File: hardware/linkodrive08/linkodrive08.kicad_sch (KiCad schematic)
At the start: 146 parts, among them J1 USB_C_Receptacle_USB2.0_16P, J10 WCH_GPIO, J11 ENC, J12 LKS_SPI, J13 LKS_I2C, J14 WCH_UART_ALT, J15 LKS_SIF, J16 LKS_IO, J2 HALL, J3 WCH_SWD, J4 LKS_SWD, J5 MOT_POWER, J6 GATE_DRIVE, J7 LOGIC_POWER, J8 MOT, J9 CAN, Q1 HSU6066, Q2 HSU6066, Q3 HSU6066, Q4 HSU6066, Q5 HSU6066, Q6 HSU6066, U1 LKS32MC086NxQx, U2 CH32V203G6U6, U3 XL1509-ADJ, U4 SN65HVD230, U5 LGS5145, Y1 Crystal_GND24_Small

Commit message: Work on pcb and some parts changes
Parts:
- C33, C34, C35: footprint MISSING -> Capacitor_SMD:C_Elec_10x10.2
- D1, D10, D4, D7: value SS34 -> C28646289; footprint Diode_SMD:D_SMA -> Diode_SMD:D_SOD-123F; LCSC C8678 -> C28646289
- D2, D3, D5, D6, D8, D9: value ES2DB -> ES2JW; footprint Diode_SMD:D_SMB -> Diode_SMD:D_SOD-123F; LCSC C162764 -> C353499
- Q1, Q2, Q3, Q4, Q5, Q6: footprint Package_TO_SOT_SMD:TO-252-2 -> Package_SO:ONSemi_SO-8FL_488AA
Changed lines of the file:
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@@
 			)
 		)
-		(property "Footprint" "Package_TO_SOT_SMD:TO-252-2"
+		(property "Footprint" "Package_SO:ONSemi_SO-8FL_488AA"
 			(at 327.66 198.12 0)
 			(effects
@@
 			)
 		)
-		(property "Footprint" "MISSING"
+		(property "Footprint" "Capacitor_SMD:C_Elec_10x10.2"
 			(at 251.46 167.64 0)
 			(effects
@@
 			)
 		)
-		(property "Value" "SS34"
+		(property "Value" "C28646289"
 			(at 285.75 181.61 0)
 			(effects
@@
 			)
 		)
-		(property "Footprint" "Diode_SMD:D_SMA"
+		(property "Footprint" "Diode_SMD:D_SOD-123F"
 			(at 280.67 184.15 90)
 			(effects
@@
 			)
 		)
-		(property "LCSC" "C8678"
+		(property "LCSC" "C28646289"
 			(at 280.67 184.15 90)
 			(effects
@@
 			)
 		)
-		(property "Value" "ES2DB"
+		(property "Value" "ES2JW"
 			(at 294.132 211.074 0)
 			(effects
@@
 			)
 		)
-		(property "Footprint" "Diode_SMD:D_SMB"
+		(property "Footprint" "Diode_SMD:D_SOD-123F"
 			(at 297.18 213.36 90)
 			(effects
@@
 			)
 		)
-		(property "LCSC" "C162764"
+		(property "LCSC" "C353499"
 			(at 297.18 213.36 0)
 			(effects
@@
 			)
 		)
-		(property "Value" "ES2DB"
+		(property "Value" "ES2JW"
 			(at 167.132 264.414 0)
 			(effects
@@
 			)
 		)
-		(property "Footprint" "Diode_SMD:D_SMB"
+		(property "Footprint" "Diode_SMD:D_SOD-123F"
 			(at 170.18 266.7 90)
 			(effects
@@
 			)
 		)
-		(property "LCSC" "C162764"
+		(property "LCSC" "C353499"
 			(at 170.18 266.7 0)
 			(effects
@@
 			)
 		)
-		(property "Footprint" "Package_TO_SOT_SMD:TO-252-2"
+		(property "Footprint" "Package_SO:ONSemi_SO-8FL_488AA"
 			(at 200.66 264.16 0)
 			(effects
@@
 			)
 		)
-		(property "Value" "ES2DB"
+		(property "Value" "ES2JW"
 			(at 165.862 211.074 0)
 			(effects
@@
 			)
 		)
-		(property "Footprint" "Diode_SMD:D_SMB"
+		(property "Footprint" "Diode_SMD:D_SOD-123F"
 			(at 168.91 213.36 90)
 			(effects
@@
 			)
 		)
-		(property "LCSC" "C162764"
+		(property "LCSC" "C353499"
 			(at 168.91 213.36 0)
 			(effects
@@
 			)
 		)
-		(property "Footprint" "Package_TO_SOT_SMD:TO-252-2"
+		(property "Footprint" "Package_SO:ONSemi_SO-8FL_488AA"
 			(at 327.66 210.82 0)
 			(effects
@@
 			)
 		)
-		(property "Value" "SS34"
+		(property "Value" "C28646289"
 			(at 358.902 49.784 90)
 			(effects
@@
 			)
 		)
-		(property "Footprint" "Diode_SMD:D_SMA"
+		(property "Footprint" "Diode_SMD:D_SOD-123F"
 			(at 355.6 48.26 90)
 			(effects
@@
 			)
 		)
-		(property "LCSC" "C8678"
+		(property "LCSC" "C28646289"
 			(at 355.6 48.26 90)
 			(effects
@@
 			)
 		)
-		(property "Footprint" "MISSING"
+		(property "Footprint" "Capacitor_SMD:C_Elec_10x10.2"
 			(at 227.33 167.64 0)
 			(effects
@@
 			)
 		)
-		(property "Value" "ES2DB"
+		(property "Value" "ES2JW"
 			(at 295.402 198.374 0)
 			(effects
@@
 			)
 		)
-		(property "Footprint" "Diode_SMD:D_SMB"
+		(property "Footprint" "Diode_SMD:D_SOD-123F"
 			(at 297.18 200.66 90)
 			(effects
@@
 			)
 		)
-		(property "LCSC" "C162764"
+		(property "LCSC" "C353499"
 			(at 297.18 200.66 0)
 			(effects
@@
 			)
 		)
-		(property "Footprint" "Package_TO_SOT_SMD:TO-252-2"
+		(property "Footprint" "Package_SO:ONSemi_SO-8FL_488AA"
 			(at 199.39 198.12 0)
 			(effects
@@
 			)
 		)
-		(property "Footprint" "MISSING"
+		(property "Footprint" "Capacitor_SMD:C_Elec_10x10.2"
 			(at 240.03 167.64 0)
 			(effects
@@
 			)
 		)
-		(property "Value" "SS34"
+		(property "Value" "C28646289"
 			(at 158.75 234.95 0)
 			(effects
@@
 			)
 		)
-		(property "Footprint" "Diode_SMD:D_SMA"
+		(property "Footprint" "Diode_SMD:D_SOD-123F"
 			(at 153.67 237.49 90)
 			(effects
@@
 			)
 		)
-		(property "LCSC" "C8678"
+		(property "LCSC" "C28646289"
 			(at 153.67 237.49 90)
 			(effects
@@
 			)
 		)
-		(property "Footprint" "Package_TO_SOT_SMD:TO-252-2"
+		(property "Footprint" "Package_SO:ONSemi_SO-8FL_488AA"
 			(at 200.66 251.46 0)
 			(effects
@@
 			)
 		)
-		(property "Value" "SS34"
+		(property "Value" "C28646289"
 			(at 157.48 181.61 0)
 			(effects
@@
 			)
 		)
-		(property "Footprint" "Diode_SMD:D_SMA"
+		(property "Footprint" "Diode_SMD:D_SOD-123F"
 			(at 152.4 184.15 90)
 			(effects
@@
 			)
 		)
-		(property "LCSC" "C8678"
+		(property "LCSC" "C28646289"
 			(at 152.4 184.15 90)
 			(effects
@@
 			)
 		)
-		(property "Value" "ES2DB"
+		(property "Value" "ES2JW"
 			(at 167.132 198.374 0)
 			(effects
@@
 			)
 		)
-		(property "Footprint" "Diode_SMD:D_SMB"
+		(property "Footprint" "Diode_SMD:D_SOD-123F"
 			(at 168.91 200.66 90)
 			(effects
@@
 			)
 		)
-		(property "LCSC" "C162764"
+		(property "LCSC" "C353499"
 			(at 168.91 200.66 0)
 			(effects
@@
 			)
 		)
-		(property "Footprint" "Package_TO_SOT_SMD:TO-252-2"
+		(property "Footprint" "Package_SO:ONSemi_SO-8FL_488AA"
 			(at 199.39 210.82 0)
 			(effects
@@
 			)
 		)
-		(property "Value" "ES2DB"
+		(property "Value" "ES2JW"
 			(at 168.402 251.714 0)
 			(effects
@@
 			)
 		)
-		(property "Footprint" "Diode_SMD:D_SMB"
+		(property "Footprint" "Diode_SMD:D_SOD-123F"
 			(at 170.18 254 90)
 			(effects
@@
 			)
 		)
-		(property "LCSC" "C162764"
+		(property "LCSC" "C353499"
 			(at 170.18 254 0)
 			(effects

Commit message: more work on PCB
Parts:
- added Q7: DMN3008SFG, Package_SON:Diodes_PowerDI3333-8, symbol Transistor_FET:DMN3008SFG
- D1, D10, D4, D7: value C28646289 -> DSK310
- U2: footprint Package_DFN_QFN:QFN-28-1EP_4x4mm_P0.4mm_EP2.6x2.6mm -> Package_DFN_QFN:QFN-28-1EP_4x4mm_P0.4mm_EP2.6x2.6mm_ThermalVias
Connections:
- new net: Q7.1 (S), Q7.2 (S), Q7.3 (S)
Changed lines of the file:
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@@
 			)
 		)
-		(property "Value" "C28646289"
+		(property "Value" "DSK310"
 			(at 285.75 181.61 0)
 			(effects
@@
 		)
 		(instances
-			(project ""
+			(project "linkodrive08"
 				(path "/1d70325a-38b2-49fb-b3a9-bb06bd833a17"
 					(reference "R44")
@@
 	)
 	(symbol
+		(lib_id "Transistor_FET:DMN3008SFG")
+		(at 330.2 184.15 0)
+		(unit 1)
+		(exclude_from_sim no)
+		(in_bom yes)
+		(on_board yes)
+		(dnp no)
+		(fields_autoplaced yes)
+		(property "Reference" "Q7"
+			(at 336.55 182.8799 0)
+			(effects
+				(font
+					(size 1.27 1.27)
+				)
+				(justify left)
+			)
+		)
+		(property "Value" "DMN3008SFG"
+			(at 336.55 185.4199 0)
+			(effects
+				(font
+					(size 1.27 1.27)
+				)
+				(justify left)
+			)
+		)
+		(property "Footprint" "Package_SON:Diodes_PowerDI3333-8"
+			(at 335.28 186.055 0)
+			(effects
+				(font
+					(size 1.27 1.27)
+					(italic yes)
+				)
+				(justify left)
+				(hide yes)
+			)
+		)
+		(property "Datasheet" "https://www.diodes.com/assets/Datasheets/DMN3008SFG.pdf"
+			(at 335.28 187.96 0)
+			(effects
+				(font
+					(size 1.27 1.27)
+				)
+				(justify left)
+				(hide yes)
+			)
+		)
+		(property "Description" "17.6A Id, 30V Vds, N-Channel Power MOSFET, 4.4mOhm Ron, 86nC Qg (typ), PowerDI3333-8"
+			(at 330.2 184.15 0)
+			(effects
+				(font
+					(size 1.27 1.27)
+				)
+				(hide yes)
+			)
+		)
+		(pin "3"
+		)
+		(pin "4"
+		)
+		(pin "2"
+		)
+		(pin "1"
+		)
+		(pin "5"
+		)
+		(instances
+			(project "linkodrive08"
+				(path "/1d70325a-38b2-49fb-b3a9-bb06bd833a17"
+					(reference "Q7")
+					(unit 1)
+				)
+			)
+		)
+	)
+	(symbol
 		(lib_id "Device:R_Small")
 		(at 346.71 224.79 270)
@@
 			)
 		)
-		(property "Value" "C28646289"
+		(property "Value" "DSK310"
 			(at 358.902 49.784 90)
 			(effects
@@
 			)
 		)
-		(property "Footprint" "Package_DFN_QFN:QFN-28-1EP_4x4mm_P0.4mm_EP2.6x2.6mm"
+		(property "Footprint" "Package_DFN_QFN:QFN-28-1EP_4x4mm_P0.4mm_EP2.6x2.6mm_ThermalVias"
 			(at 166.37 49.53 0)
 			(effects
@@
 		)
 		(instances
-			(project ""
+			(project "linkodrive08"
 				(path "/1d70325a-38b2-49fb-b3a9-bb06bd833a17"
 					(reference "C33")
@@
 			)
 		)
-		(property "Value" "C28646289"
-			(at 158.75 234.95 0)
+		(property "Value" "DSK310"
+			(at 159.258 234.95 0)
 			(effects
 				(font
@@
 			)
 		)
-		(property "Value" "C28646289"
+		(property "Value" "DSK310"
 			(at 157.48 181.61 0)
 			(effects

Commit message: Finish layout
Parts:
- removed J5: MOT_POWER, Connector_PinSocket_2.54mm:PinSocket_1x02_P2.54mm_Vertical, symbol Connector_Generic:Conn_01x02
- removed J8: MOT, Connector_PinSocket_2.54mm:PinSocket_1x03_P2.54mm_Vertical, symbol Connector_Generic:Conn_01x03
- removed Q7: DMN3008SFG, Package_SON:Diodes_PowerDI3333-8, symbol Transistor_FET:DMN3008SFG
- added C38: Cs, Capacitor_SMD:C_0603_1608Metric, symbol Device:C_Small
- added J1: VBUS, TestPoint:TestPoint_Plated_Hole_D4.0mm, symbol Connector_Generic:Conn_01x01
- added J14: MOT_U, TestPoint:TestPoint_Plated_Hole_D4.0mm, symbol Connector_Generic:Conn_01x01
- added J15: MOT_V, TestPoint:TestPoint_Plated_Hole_D4.0mm, symbol Connector_Generic:Conn_01x01
- added J16: MOT_W, TestPoint:TestPoint_Plated_Hole_D4.0mm, symbol Connector_Generic:Conn_01x01
- added J19: GND, TestPoint:TestPoint_Plated_Hole_D4.0mm, symbol Connector_Generic:Conn_01x01
- added R46, R47: Rs, Resistor_SMD:R_0603_1608Metric, symbol Device:R_Small
- J11: renamed from J13; now not fitted
- J17: renamed from J10; now not fitted
- J7: renamed from J12; now not fitted
- J8: renamed from J9; now not fitted
- Q1: renamed from Q3; value HSU6066 -> JMTK80N06A; footprint Package_SO:ONSemi_SO-8FL_488AA -> Package_TO_SOT_SMD:TO-252-2; LCSC C22359249 -> C3031548
- Q2: renamed from Q4; value HSU6066 -> JMTK80N06A; footprint Package_SO:ONSemi_SO-8FL_488AA -> Package_TO_SOT_SMD:TO-252-2; LCSC C22359249 -> C3031548
- Q3: renamed from Q1; value HSU6066 -> JMTK80N06A; footprint Package_SO:ONSemi_SO-8FL_488AA -> Package_TO_SOT_SMD:TO-252-2; LCSC C22359249 -> C3031548
- Q4: renamed from Q2; value HSU6066 -> JMTK80N06A; footprint Package_SO:ONSemi_SO-8FL_488AA -> Package_TO_SOT_SMD:TO-252-2; LCSC C22359249 -> C3031548
- Q5, Q6: value HSU6066 -> JMTK80N06A; footprint Package_SO:ONSemi_SO-8FL_488AA -> Package_TO_SOT_SMD:TO-252-2; LCSC C22359249 -> C3031548
- U2: renamed from U4; now fitted
- renumbered C29 to C10, C5 to C13, C7 to C14, C28 to C15, C2 to C16, C3 to C17, C25 to C18, C24 to C19, C37 to C2, C33 to C20, C13 to C21, C8 to C22, C34 to C23, C35 to C24, C36 to C25, C14 to C26, C30 to C27, C15 to C28, C19 to C29, C9 to C3, C16 to C30, C17 to C31, C22 to C32, C26 to C33, C21 to C34, C18 to C35, C20 to C36, C23 to C37, C10 to C5, C27 to C7, C31 to C8, C32 to C9, D12 to D1, D8 to D10, D9 to D11, D10 to D12, D11 to D13, D13 to D2, D4 to D3, D1 to D4, D2 to D7, D3 to D8, D7 to D9, J11 to J10, J4 to J12, J2 to J13, J14 to J18, J1 to J2, J6 to J3, J7 to J4, J15 to J5, J16 to J6, J3 to J9, NT9 to NT1, NT7 to NT10, NT8 to NT11, NT10 to NT2, NT1 to NT3, NT2 to NT4, NT3 to NT5, NT4 to NT6, NT5 to NT7, NT6 to NT8, NT11 to NT9, R45 to R1, R5 to R10, R16 to R11, R19 to R12, R7 to R13, R9 to R14, R17 to R16, R6 to R17, R8 to R18, R21 to R19, R1 to R2, R10 to R20, R36 to R21, R37 to R22, R32 to R23, R35 to R24, R18 to R25, R20 to R26, R11 to R27, R12 to R28, R4 to R29, R2 to R3, R43 to R30, R13 to R31, R22 to R32, R24 to R33, R27 to R34, R23 to R35, R25 to R36, R29 to R37, R39 to R38, R40 to R39, R44 to R4, R26 to R40, R28 to R41, R30 to R42, R31 to R43, R33 to R44, R34 to R45, R38 to R5, R41 to R6, R42 to R7, R3 to R8, R14 to R9, TP3 to TP1, TP4 to TP2, TP5 to TP3, TP6 to TP4, TP2 to TP5, TP1 to TP6, U2 to U3, U3 to U4
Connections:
- net GND: now also J19.1 (Pin_1)
- net ISENSE_TOT+: now also C38.1, R46.1; no longer NT8.2
- net ISENSE_TOT-: now also C38.2, R47.1; no longer NT7.1
- net MOT1: now also J14.1 (Pin_1); no longer R40.1
- net MOT2: now also J15.1 (Pin_1); no longer R25.1
- net MOT3: now also J16.1 (Pin_1); no longer R27.1
- net VBUS: now also J1.1 (Pin_1)
- net VS1 renamed MOT1_MEAS
- net MOT1_MEAS: now also R40.1
- net VS2 renamed MOT2_MEAS
- net MOT2_MEAS: now also R25.1
- net VS3 renamed MOT3_MEAS
- net MOT3_MEAS: now also R27.1
- new net P_IST+: NT8.2, R46.2
- new net P_IST-: NT7.1, R47.2
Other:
- note added: "Motor Out"
- note added: "Possible other transistor options: - HSU6066 - C22359249 - TO-252 - WSD4070DN - C719095 - DFN3X3-8L - JMTK80N06A - C3031548 - TO-252-4R"
- note removed: "Motor Out (split?)"
- note removed: "Possible other transistor options: - HSU6066 - C22359249 - WSD4070DN - C719095"
- moved on the sheet: R31

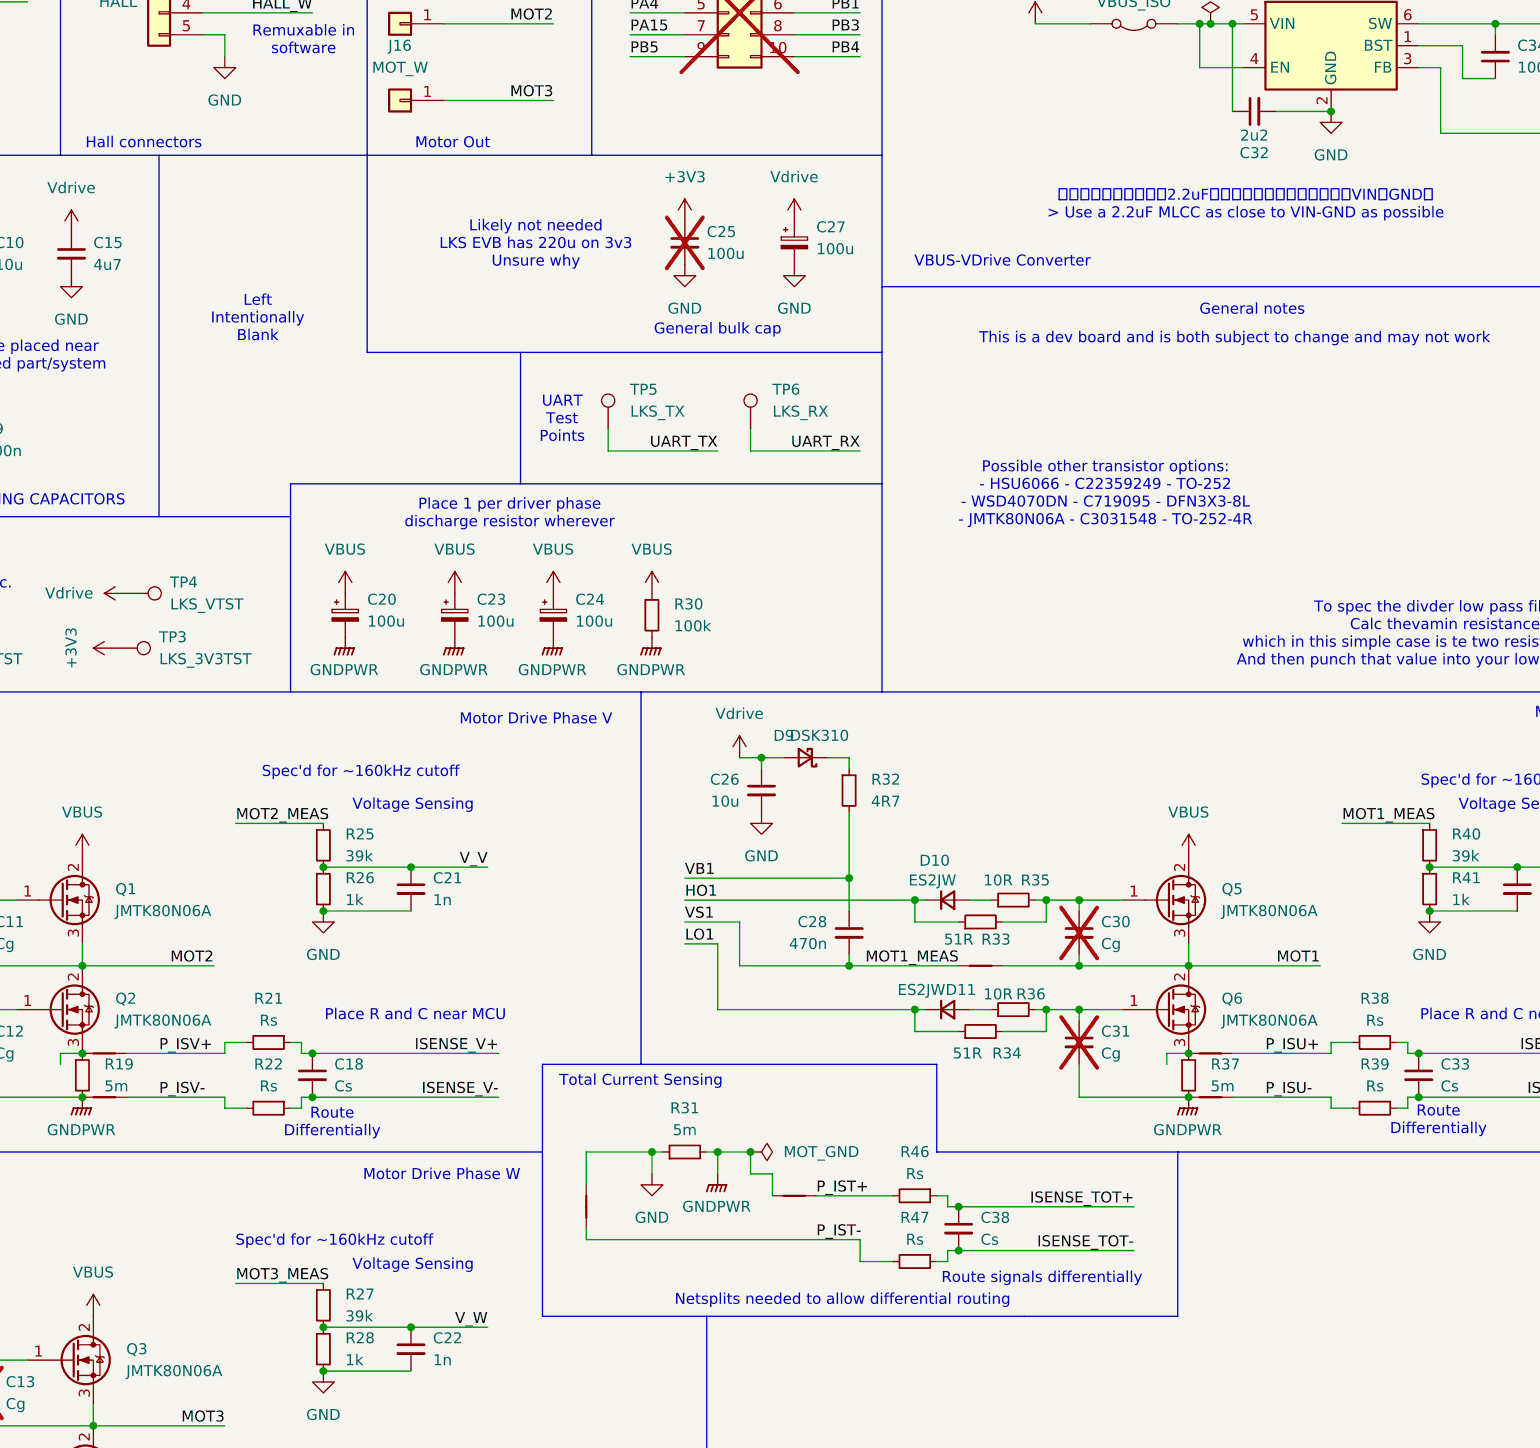
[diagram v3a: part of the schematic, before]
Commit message: Add power indicator LEDs
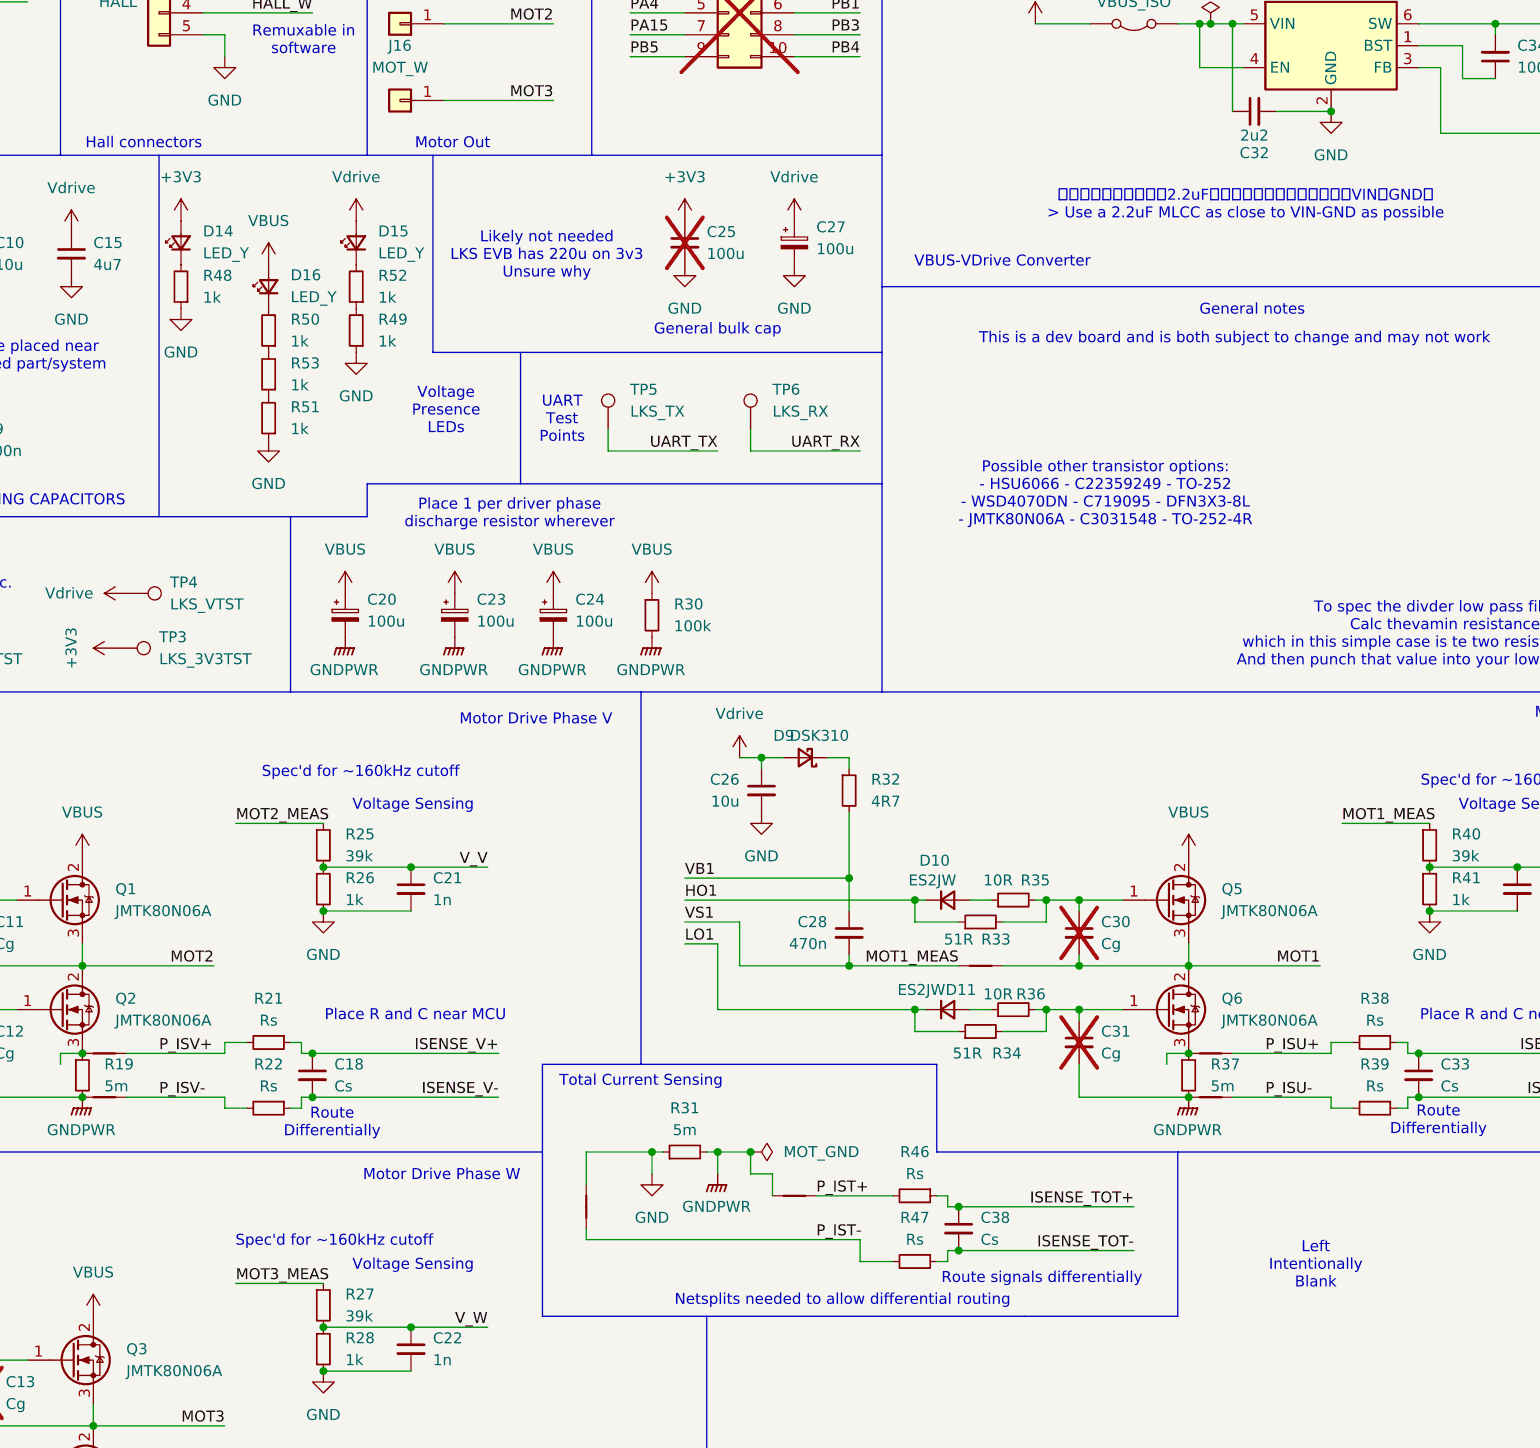
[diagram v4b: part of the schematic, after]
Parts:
- added D14, D15, D16: LED_Y, LED_SMD:LED_0603_1608Metric, symbol Device:LED_Small
- added R48, R49, R50, R51, R52, R53: 1k, Resistor_SMD:R_0603_1608Metric, symbol Device:R_Small
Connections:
- net +3V3: now also D14.2 (A)
- net GND: now also R48.1, R49.1, R51.1
- net VBUS: now also D16.2 (A)
- net Vdrive: now also D15.2 (A)
- new net: R49.2, R52.1
- new net: R51.2, R53.1
- new net: R50.1, R53.2
- new net: D14.1 (K), R48.2
- new net: D15.1 (K), R52.2
- new net: D16.1 (K), R50.2
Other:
- note added: "Voltage Presence LEDs"

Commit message: changes?
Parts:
- C27: LCSC C72478 -> C5155339
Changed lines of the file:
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@@
 			)
 		)
-		(property "LCSC" "C72478"
+		(property "LCSC" "C5155339"
 			(at 279.4 124.46 0)
 			(effects
